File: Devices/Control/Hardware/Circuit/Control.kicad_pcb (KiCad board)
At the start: 2 copper layers, 26 parts, among them J1 Screw_Terminal_01x03, J2 AVR-ISP-6, J3 TYPE-C-31-M-12, J4 Conn_01x13, J5 Conn_01x04, J6 Conn_01x04, J7 TYPE-C-31-M-12, U1 ATmega328P-AU, U2 CH340C, Y1 16MHz

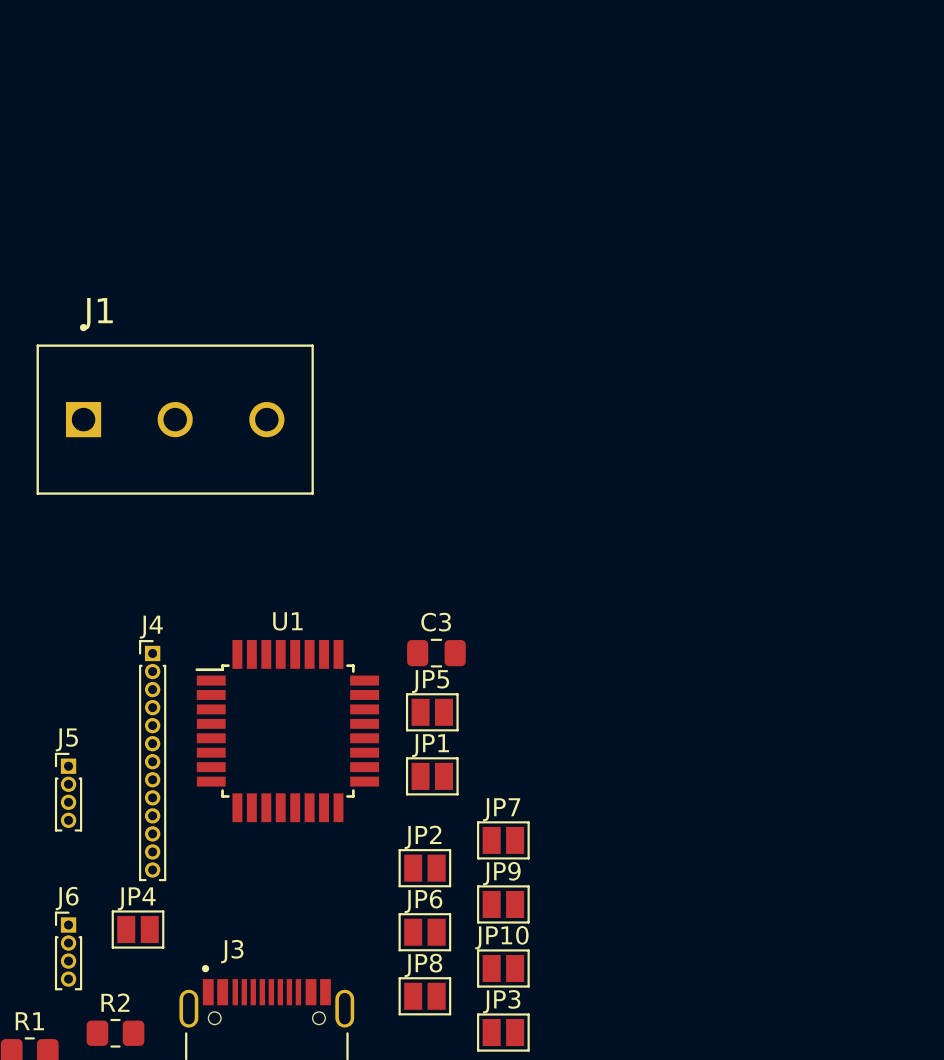
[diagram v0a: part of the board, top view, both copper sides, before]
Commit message: Add uart multiplexer
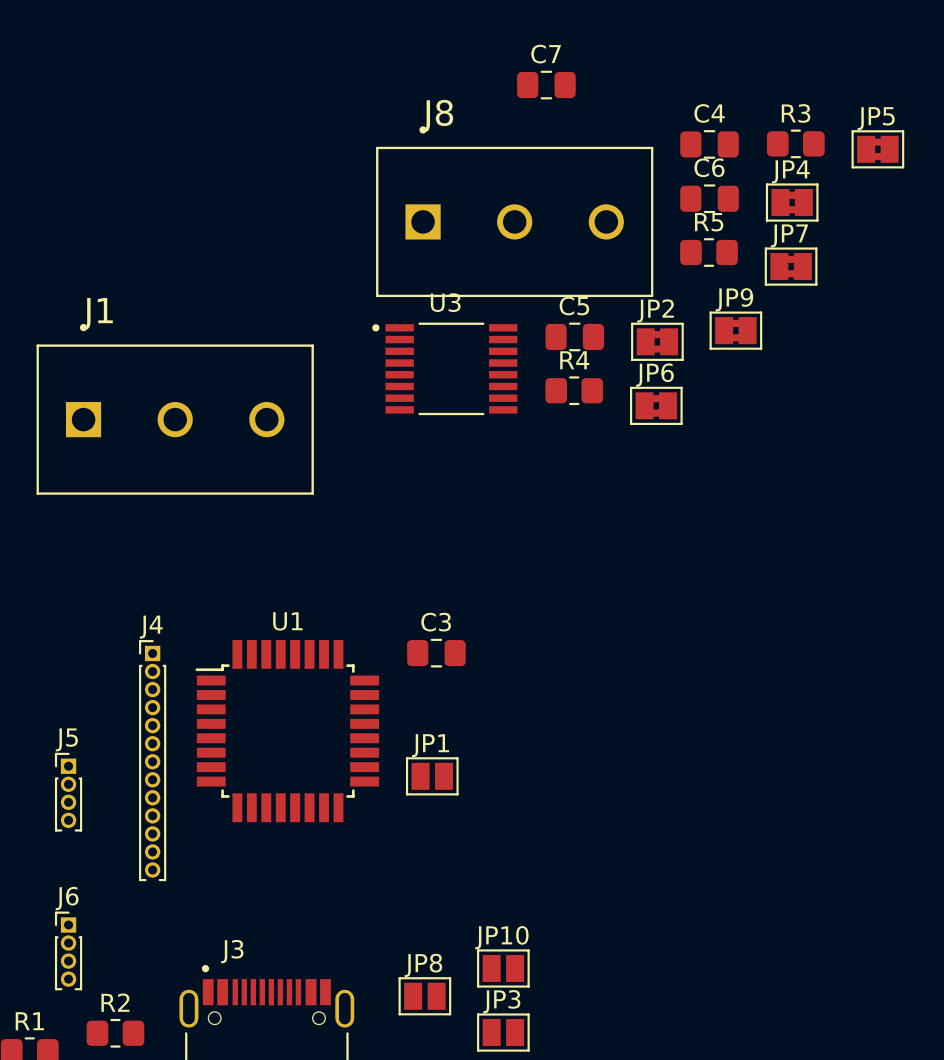
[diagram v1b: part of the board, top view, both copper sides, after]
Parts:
- added C4: 100n, Capacitor_SMD:C_0805_2012Metric_Pad1.18x1.45mm_HandSolder, F.Cu at (100.7, 133.8)
- added C5: 100n, Capacitor_SMD:C_0805_2012Metric_Pad1.18x1.45mm_HandSolder, F.Cu at (93.3, 144.5)
- added C6: 100n, Capacitor_SMD:C_0805_2012Metric_Pad1.18x1.45mm_HandSolder, F.Cu at (100.7, 136.9)
- added C7: 100n, Capacitor_SMD:C_0805_2012Metric_Pad1.18x1.45mm_HandSolder, F.Cu at (91.7, 130.6)
- added J8: Screw_Terminal_01x03, CUI_TB006-508-03BE:CUI_TB006-508-03BE, F.Cu at (84.9, 138.1)
- added R3: 120, Resistor_SMD:R_0805_2012Metric_Pad1.20x1.40mm_HandSolder, F.Cu at (105.5, 133.8)
- added R4: 40.2, Resistor_SMD:R_0805_2012Metric_Pad1.20x1.40mm_HandSolder, F.Cu at (93.2, 147.5)
- added R5: 40.2, Resistor_SMD:R_0805_2012Metric_Pad1.20x1.40mm_HandSolder, F.Cu at (100.7, 139.8)
- added U3: CD74HC4053PWR, CD74HC4053PWR:SOP65P640X120-16N, F.Cu at (86.4, 146.3)
- JP2, JP4, JP5, JP6, JP7, JP9: value SolderJumper -> SolderJumper_Bridged; footprint Jumper:SolderJumper-2_P1.3mm_Open_Pad1.0x1.5mm -> Jumper:SolderJumper-2_P1.3mm_Bridged2Bar_Pad1.0x1.5mm
- moved JP4 54.2 mm to (105.3, 137.1)
- moved JP5 39.8 mm to (110.1, 134.1)
- moved JP7 35.6 mm to (105.3, 140.6)
- moved JP9 34.3 mm to (102.2, 144.2)
- moved JP2 31.9 mm to (97.8, 144.8)
- moved JP6 31.9 mm to (97.8, 148.3)
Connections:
- J1 pad 1: Net-(J1-Pad1) -> SIG1A
- J1 pad 2: Net-(J1-Pad2) -> SIG1B
- J1 pad 3: Net-(J1-Pad3) -> GND
- J3 pad A4B9: VCC -> Net-(J3-PadA4B9)
- J3 pad B4A9: VCC -> Net-(J3-PadB4A9)
- J5 pad 2: RX -> TX
- J5 pad 3: TX -> RX
- J7 pad A1B12: Net-(J7-PadA1B12) -> GND
- J7 pad A4B9: Net-(J7-PadA4B9) -> VCC
- J7 pad A6: Net-(J7-PadA6) -> D+
- J7 pad A7: Net-(J7-PadA7) -> D-
- J7 pad B1A12: Net-(J7-PadB1A12) -> GND
- J7 pad B4A9: Net-(J7-PadB4A9) -> VCC
- J7 pad B6: Net-(J7-PadB6) -> D+
- J7 pad B7: Net-(J7-PadB7) -> D-
- J7 pad S1: Net-(J7-PadS1) -> GND
- J7 pad S2: Net-(J7-PadS2) -> GND
- J7 pad S3: Net-(J7-PadS3) -> GND
- J7 pad S4: Net-(J7-PadS4) -> GND
- JP6 pad 1: RST -> Net-(J3-PadB8)
- JP6 pad 2: Net-(J3-PadB8) -> RST
- JP7 pad 1: TX -> Net-(J3-PadB7)
- JP7 pad 2: Net-(J3-PadB7) -> TX
- JP9 pad 1: RX -> Net-(J3-PadB6)
- JP9 pad 2: Net-(J3-PadB6) -> RX
- U1 pad 1: ENC1B -> Net-(U1-Pad1)
- U1 pad 10: ENC3A -> SIG2B
- U1 pad 11: ENC3B -> Net-(U1-Pad11)
- U1 pad 12: ENC4A -> Net-(U1-Pad12)
- U1 pad 13: ENC4B -> SIG1A
- U1 pad 14: Net-(U1-Pad14) -> SIG1B
- U1 pad 2: ENC2A -> Net-(U1-Pad2)
- U1 pad 23: BTN1 -> Net-(U1-Pad23)
- U1 pad 24: BTN2 -> Net-(U1-Pad24)
- U1 pad 25: BTN3 -> Net-(U1-Pad25)
- U1 pad 26: BTN4 -> Net-(U1-Pad26)
- U1 pad 32: ENC1A -> Net-(U1-Pad32)
- U1 pad 9: ENC2B -> SIG2A
- U2 pad 1: Net-(U2-Pad1) -> GND
- U2 pad 16: Net-(U2-Pad16) -> VCC
- U2 pad 2: Net-(U2-Pad2) -> RX
- U2 pad 3: Net-(U2-Pad3) -> TX
- U2 pad 5: Net-(U2-Pad5) -> D+
- U2 pad 6: Net-(U2-Pad6) -> D-

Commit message: Add console UART muxing
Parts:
- added R6: 10k, Resistor_SMD:R_0805_2012Metric_Pad1.20x1.40mm_HandSolder, F.Cu at (49.4, 125.9)
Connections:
- C6 pad 1: RST -> ICRST
- JP2 pad 1: RX -> EXTRX
- JP4 pad 1: TX -> EXTTX
- JP5 pad 1: RST -> EXTRST
- JP6 pad 2: RST -> EXTRST
- JP7 pad 2: TX -> EXTTX
- JP9 pad 2: RX -> EXTRX
- U1 pad 1: Net-(U1-Pad1) -> MUXS1
- U1 pad 2: Net-(U1-Pad2) -> MUXS2
- U1 pad 32: Net-(U1-Pad32) -> MUXS0
- U2 pad 2: RX -> ICTX
- U2 pad 3: TX -> ICRX
- U3 pad 1: Net-(U3-Pad1) -> EXTTX
- U3 pad 10: Net-(U3-Pad10) -> MUXS1
- U3 pad 11: Net-(U3-Pad11) -> MUXS0
- U3 pad 12: Net-(U3-Pad12) -> RX
- U3 pad 13: Net-(U3-Pad13) -> EXTRX
- U3 pad 14: Net-(U3-Pad14) -> ICTX
- U3 pad 15: Net-(U3-Pad15) -> ICRX
- U3 pad 16: Net-(U3-Pad16) -> VCC
- U3 pad 2: Net-(U3-Pad2) -> TX
- U3 pad 3: Net-(U3-Pad3) -> EXTRST
- U3 pad 4: Net-(U3-Pad4) -> ICRST
- U3 pad 5: Net-(U3-Pad5) -> RST
- U3 pad 7: Net-(U3-Pad7) -> GND
- U3 pad 8: Net-(U3-Pad8) -> GND
- U3 pad 9: Net-(U3-Pad9) -> MUXS2

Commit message: Add control reset functionality
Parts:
- added D2: 17-21/BHC-XL2M2TY/3T, LED_SMD:LED_0805_2012Metric_Castellated, F.Cu at (31.2, 132.4)
- added Q1: Q_NPN_BCE, Package_TO_SOT_SMD:SOT-23_Handsoldering, F.Cu at (70.4, 128.0)
- added SW1: SW_Push, SKRKAEE020:SKRKAEE020, F.Cu at (32.8, 128.0)
- added SW2: SW_Push, SKRKAEE020:SKRKAEE020, F.Cu at (40.9, 128.0)
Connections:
- R3 pad 1: Net-(R3-Pad1) -> RST
- U1 pad 11: Net-(U1-Pad11) -> STOPRST-SIG
- U1 pad 12: Net-(U1-Pad12) -> STOPRST

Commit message: Restructure control schematic
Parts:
- added JP11: SolderJumper, Jumper:SolderJumper-2_P1.3mm_Open_Pad1.0x1.5mm, F.Cu at (14.4, 141.7)
- added JP12: SolderJumper_Bridged, Jumper:SolderJumper-2_P1.3mm_Bridged2Bar_Pad1.0x1.5mm, F.Cu at (14.4, 145.3)
- added JP13: SolderJumper, Jumper:SolderJumper-2_P1.3mm_Open_Pad1.0x1.5mm, F.Cu at (18.7, 141.7)
- added JP14: SolderJumper_Bridged, Jumper:SolderJumper-2_P1.3mm_Bridged2Bar_Pad1.0x1.5mm, F.Cu at (18.7, 145.3)
- added JP15: SolderJumper, Jumper:SolderJumper-2_P1.3mm_Open_Pad1.0x1.5mm, F.Cu at (23.1, 141.7)
- added JP16: SolderJumper_Bridged, Jumper:SolderJumper-2_P1.3mm_Bridged2Bar_Pad1.0x1.5mm, F.Cu at (23.1, 145.3)
- added R7: 1k, Resistor_SMD:R_0805_2012Metric_Pad1.20x1.40mm_HandSolder, F.Cu at (63.6, 132.8)
- J4: value Conn_01x13 -> Conn_01x04; footprint Connector_PinHeader_1.00mm:PinHeader_1x13_P1.00mm_Vertical -> Connector_PinHeader_1.00mm:PinHeader_1x04_P1.00mm_Vertical
- U1: value ATmega328P-AU -> ATmega328PB-AU
- moved U1 41.6 mm to (55.4, 131.1)
- moved J4 36.0 mm to (62.9, 126.8)
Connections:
- C6 pad 1: ICRST -> Net-(C6-Pad1)
- J2 pad 1: MISO -> EXTTX
- J2 pad 4: MOSI -> EXTRX
- J4 pad 2: ENC1A -> EXTTX
- J4 pad 3: ENC1B -> EXTRX
- J4 pad 4: ENC2A -> EXTRST
- Q1 pad 1: STOPRST -> Net-(Q1-Pad1)
- SW1 pad 1: STOPRST-SIG -> STOPRST-BTN
- U1 pad 11: STOPRST-SIG -> Net-(U1-Pad11)
- U1 pad 12: STOPRST -> Net-(U1-Pad12)
- U1 pad 15: MOSI -> EXTRX
- U1 pad 16: MISO -> EXTTX
- U1 pad 23: Net-(U1-Pad23) -> STOPRST
- U1 pad 24: Net-(U1-Pad24) -> STOPRST-BTN
- U1 pad 3: GND -> Net-(U1-Pad3)
- U1 pad 6: VCC -> Net-(U1-Pad6)
- U2 pad 13: Net-(U2-Pad13) -> Net-(C6-Pad2)
- U2 pad 14: Net-(C6-Pad2) -> Net-(U2-Pad14)
- U2 pad 2: ICTX -> Net-(JP11-Pad1)
- U2 pad 3: ICRX -> Net-(JP13-Pad1)
- U3 pad 1: EXTTX -> EXTRX
- U3 pad 12: RX -> TX
- U3 pad 13: EXTRX -> EXTTX
- U3 pad 14: ICTX -> MUXTX
- U3 pad 15: ICRX -> MUXRX
- U3 pad 2: TX -> RX
- U3 pad 4: ICRST -> MUXRST

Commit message: Add status led to control
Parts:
- added D3: 17-21/BHC-XL2M2TY/3T, LED_SMD:LED_0805_2012Metric_Castellated, F.Cu at (15.4, 127.7)
- added R8: 200, Resistor_SMD:R_0805_2012Metric_Pad1.20x1.40mm_HandSolder, F.Cu at (20.2, 127.7)
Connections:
- U1 pad 11: Net-(U1-Pad11) -> LED

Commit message: Add input serial mux & Change pin header footprint
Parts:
- added C8: 100n, Capacitor_SMD:C_0805_2012Metric_Pad1.18x1.45mm_HandSolder, F.Cu at (32.1, 120.3)
- added R9: 10k, Resistor_SMD:R_0805_2012Metric_Pad1.20x1.40mm_HandSolder, F.Cu at (41.4, 113.8)
- added U4: CD74HC4053PWR, CD74HC4053PWR:SOP65P640X120-16N, F.Cu at (34.6, 115.6)
- J4, J5, J6: footprint Connector_PinHeader_1.00mm:PinHeader_1x04_P1.00mm_Vertical -> Connector_PinHeader_2.54mm:PinHeader_1x04_P2.54mm_Vertical
- moved J6 69.8 mm to (69.5, 107.5)
- moved J5 60.8 mm to (64.9, 107.5)
- moved J4 19.4 mm to (60.2, 107.5)
- moved J2 12.2 mm to (47.8, 168.9)
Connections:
- net MUXS0 renamed MUX1S0
- net MUXS1 renamed MUX1S1
- net MUXS2 renamed MUX1S2
- J2 pad 1: EXTTX -> MISO
- J2 pad 4: EXTRX -> MOSI
- U1 pad 15: EXTRX -> MOSI
- U1 pad 16: EXTTX -> MISO
- U1 pad 19: Net-(U1-Pad19) -> MUX2S2
- U1 pad 3: Net-(U1-Pad3) -> MUX2S0
- U1 pad 6: Net-(U1-Pad6) -> MUX2S1

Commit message: Change through-hole size
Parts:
- moved J2 4.77 mm to (43.4, 170.9)

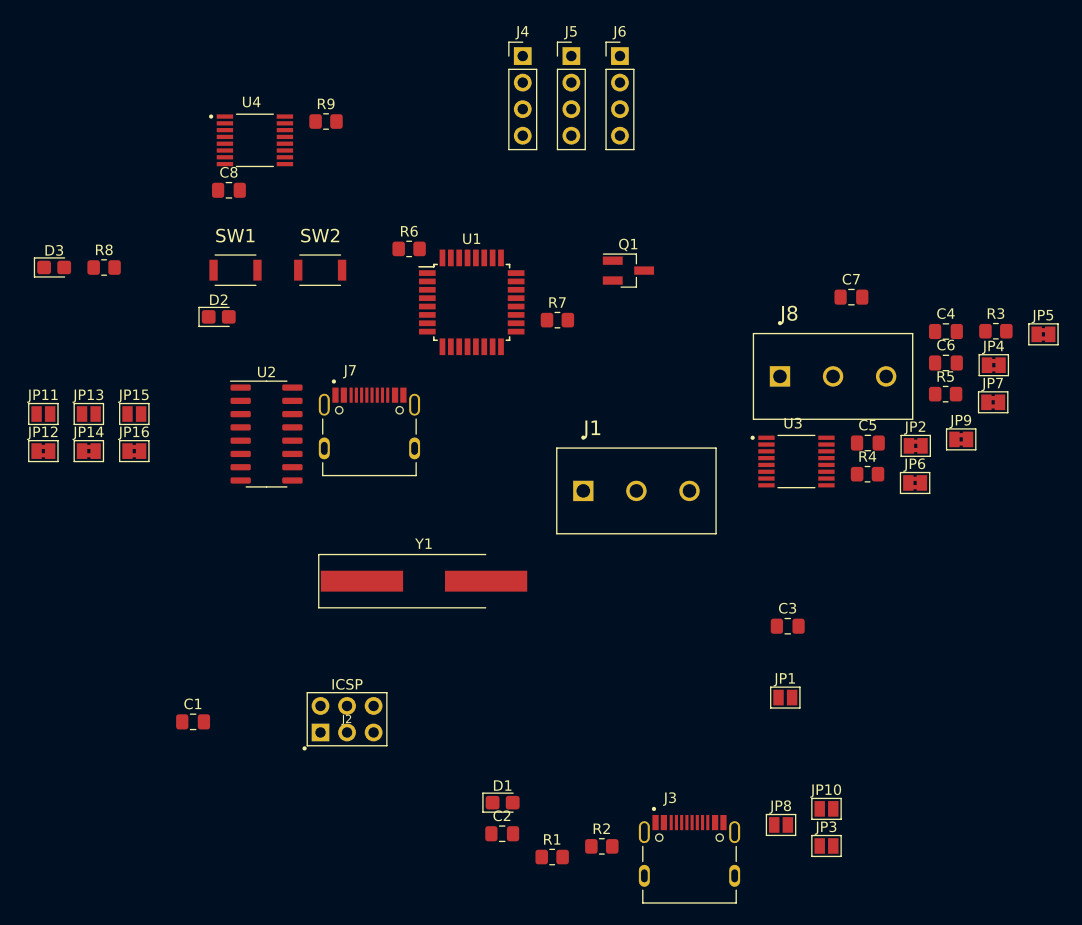
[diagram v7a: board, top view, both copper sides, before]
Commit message: Add reset hardware override
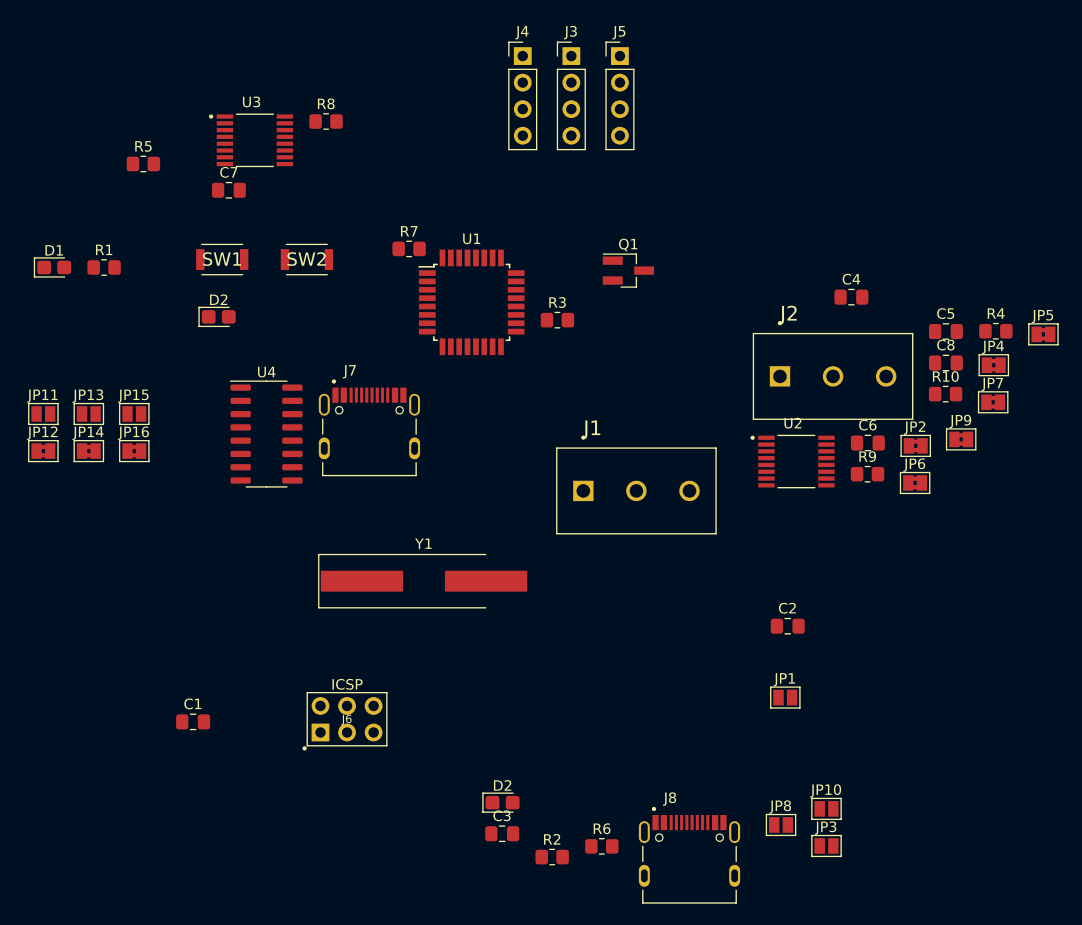
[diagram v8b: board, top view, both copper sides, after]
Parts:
- added R5: 40.2, Resistor_SMD:R_0805_2012Metric_Pad1.20x1.40mm_HandSolder, F.Cu at (23.9, 117.8)
- R3: renamed from R7; value 1k -> 40.2
- moved SW1 1.63 mm to (31.5, 127.0)
- moved SW2 1.63 mm to (39.6, 127.0)
- renumbered C3 to C2, C2 to C3, C7 to C4, C4 to C5, C5 to C6, C8 to C7, C6 to C8, D3 to D1, D1 to D2, J8 to J2, J5 to J3, J6 to J5, J2 to J6, J3 to J8, R8 to R1, R5 to R10, R1 to R2, R3 to R4, R2 to R6, R6 to R7, R9 to R8, R4 to R9, U3 to U2, U4 to U3, U2 to U4
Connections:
- D2 pad 2: Net-(D1-Pad2) (its old number) -> Net-(D2-Pad2)
- Q1 pad 3: Net-(D2-Pad2) -> Net-(Q1-Pad3)
- R4 pad 2: Net-(D2-Pad1) -> Net-(Q1-Pad3)
- R6 pad 1: Net-(D1-Pad2) (its old number) -> Net-(D2-Pad2)
- SW1 pad 1: STOPRST-BTN -> Net-(Q1-Pad3)
- SW1 pad 2: GND -> Net-(R5-Pad2)
- U1 pad 24: STOPRST-BTN -> Net-(U1-Pad24)
